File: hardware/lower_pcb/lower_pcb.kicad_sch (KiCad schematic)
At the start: 0 parts

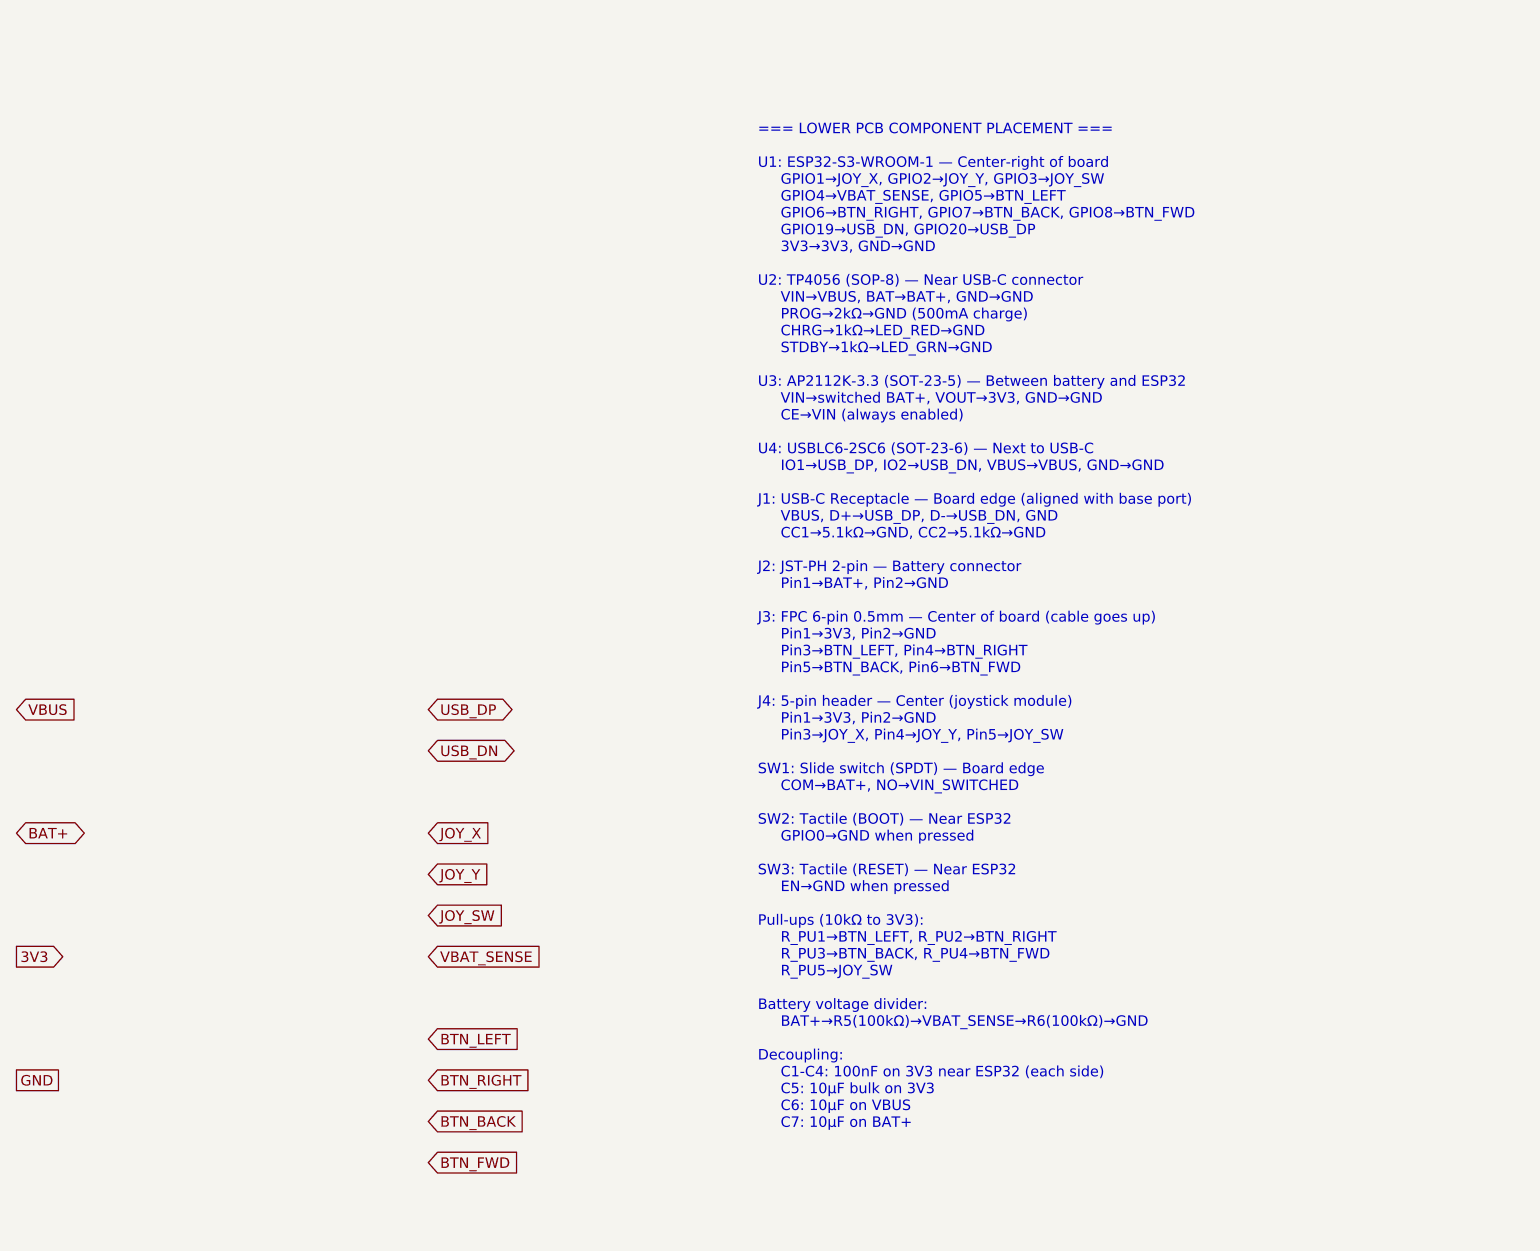
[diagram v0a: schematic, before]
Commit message: fix: move BTN pull-ups (R1-R4) to upper PCB; update schematics + BOM
- upper_pcb.kicad_sch rev 1.2: add R1-R4 (10k pull-ups) + C1 (100nF)
- lower_pcb.kicad_sch rev 1.1: remove R_PU1-R_PU4, keep R_PU5 for JOY_SW
- docs/BOM.md: updated refs to match new placement
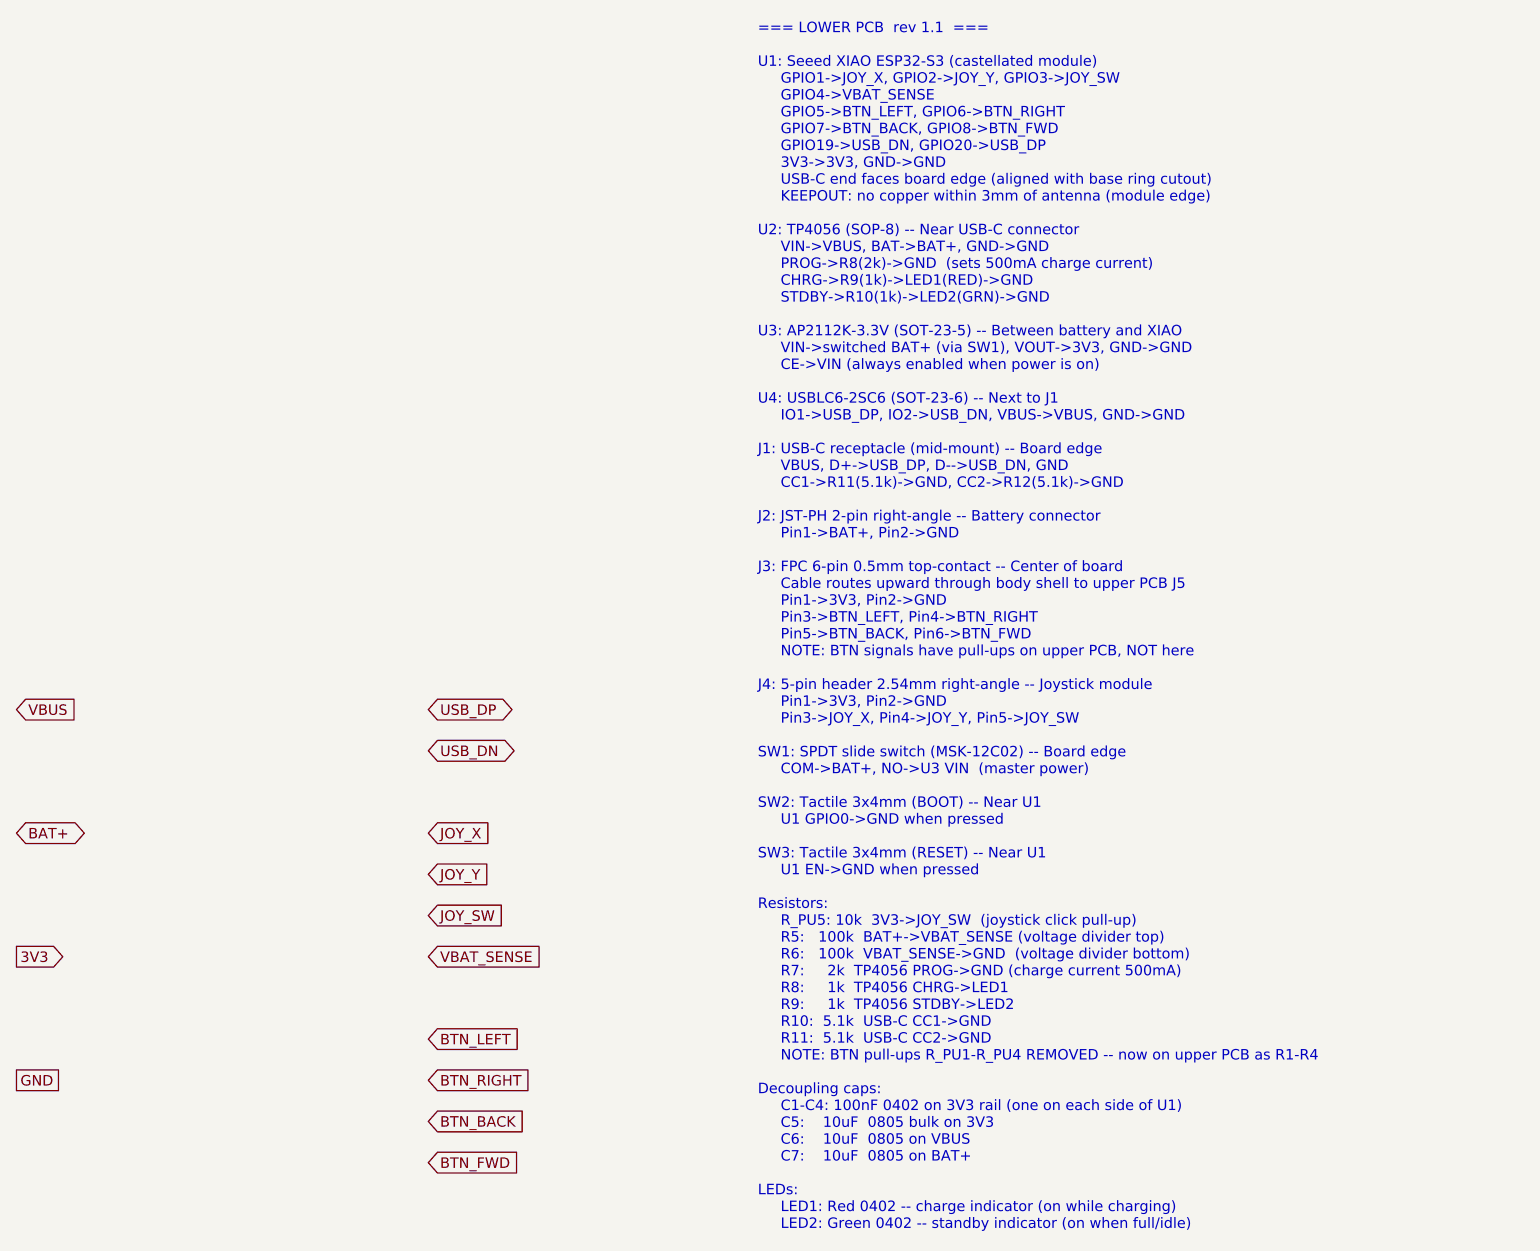
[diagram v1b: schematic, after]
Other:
- note added: "=== LOWER PCB rev 1.1 === U1: Seeed XIAO ESP32-S3 (castellated module) GPIO1->JOY_X, GPIO2->JOY_Y, GPIO3->JOY_SW GPIO4->VBAT_SENSE GPIO5->BTN_LEFT, GPIO6->BTN_RIGHT GPIO7->BTN_BACK, GPIO8->BTN_FWD GPIO19->USB_DN, GPIO20->USB_DP 3V3->3V3, GND->GND USB-C end faces board edge (aligned with base ring cutout) KEEPOUT: no copper within 3mm of antenna (module edge) U2: TP4056 (SOP-8) -- Near USB-C conne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"
- note removed: "=== LOWER PCB COMPONENT PLACEMENT === U1: ESP32-S3-WROOM-1 — Center-right of board GPIO1→JOY_X, GPIO2→JOY_Y, GPIO3→JOY_SW GPIO4→VBAT_SENSE, GPIO5→BTN_LEFT GPIO6→BTN_RIGHT, GPIO7→BTN_BACK, GPIO8→BTN_FWD GPIO19→USB_DN, GPIO20→USB_DP 3V3→3V3, GND→GND U2: TP4056 (SOP-8) — Near USB-C connector VIN→VBUS, BAT→BAT+, GND→GND PROG→2kΩ→GND (500mA charge) CHRG→1kΩ→LED_RED→GND STDBY→1kΩ→LED_GRN→GND U3: AP2112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"
- title: DaPao Space Mouse — Lower PCB -> DaPao Space Mouse - Lower PCB
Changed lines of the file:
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@@
   (paper "A3")
   (title_block
-    (title "DaPao Space Mouse — Lower PCB")
-    (date "2026-03-11")
-    (rev "1.0")
-    (comment 1 "Base board: ESP32-S3 + Power + Joystick + FPC")
-    (comment 2 "Circular PCB ∅88mm, 2-layer")
+    (title "DaPao Space Mouse - Lower PCB")
+    (date "2026-03-20")
+    (rev "1.1")
+    (comment 1 "Base board: XIAO ESP32-S3 + Power + Joystick + FPC")
+    (comment 2 "Circular PCB dia88mm, 2-layer, 1.6mm thick")
+    (comment 3 "Rev 1.1: BTN pull-ups moved to upper PCB (R1-R4). R_PU5 (JOY_SW) stays here.")
   )
-  ;; ============================================================
-  ;; This schematic defines the netlist and component references
-  ;; for the lower (base) PCB. Open in KiCad 7+ schematic editor,
-  ;; then assign footprints and place symbols interactively.
-  ;;
-  ;; Components are placed as text annotations for reference.
-  ;; Use "Place Symbol" in KiCad to add each from the library.
-  ;; ============================================================
   ;; --- POWER NETS ---
   (global_label "VBUS" (shape input) (at 30 40 0)
@@
   )
   ;; --- SIGNAL NETS ---
-  (global_label "USB_DP" (shape bidirectional) (at 80 40 0)
-    (effects (font (size 1.27 1.27)))
-  )
-  (global_label "USB_DN" (shape bidirectional) (at 80 45 0)
-    (effects (font (size 1.27 1.27)))
-  )
-  (global_label "JOY_X" (shape input) (at 80 55 0)
-    (effects (font (size 1.27 1.27)))
-  )
-  (global_label "JOY_Y" (shape input) (at 80 60 0)
-    (effects (font (size 1.27 1.27)))
-  )
-  (global_label "JOY_SW" (shape input) (at 80 65 0)
-    (effects (font (size 1.27 1.27)))
-  )
-  (global_label "VBAT_SENSE" (shape input) (at 80 70 0)
-    (effects (font (size 1.27 1.27)))
-  )
-  (global_label "BTN_LEFT" (shape input) (at 80 80 0)
-    (effects (font (size 1.27 1.27)))
-  )
-  (global_label "BTN_RIGHT" (shape input) (at 80 85 0)
-    (effects (font (size 1.27 1.27)))
-  )
-  (global_label "BTN_BACK" (shape input) (at 80 90 0)
-    (effects (font (size 1.27 1.27)))
-  )
-  (global_label "BTN_FWD" (shape input) (at 80 95 0)
-    (effects (font (size 1.27 1.27)))
-  )
-  ;; --- TEXT ANNOTATIONS (component placement guide) ---
-  (text "=== LOWER PCB COMPONENT PLACEMENT ===\n\nU1: ESP32-S3-WROOM-1 — Center-right of board\n     GPIO1→JOY_X, GPIO2→JOY_Y, GPIO3→JOY_SW\n     GPIO4→VBAT_SENSE, GPIO5→BTN_LEFT\n     GPIO6→BTN_RIGHT, GPIO7→BTN_BACK, GPIO8→BTN_FWD\n     GPIO19→USB_DN, GPIO20→USB_DP\n     3V3→3V3, GND→GND\n\nU2: TP4056 (SOP-8) — Near USB-C connector\n     VIN→VBUS, BAT→BAT+, GND→GND\n     PROG→2kΩ→GND (500mA charge)\n     CHRG→1kΩ→LED_RED→GND\n     STDBY→1kΩ→LED_GRN→GND\n\nU3: AP2112K-3.3 (SOT-23-5) — Between battery and ESP32\n     VIN→switched BAT+, VOUT→3V3, GND→GND\n     CE→VIN (always enabled)\n\nU4: USBLC6-2SC6 (SOT-23-6) — Next to USB-C\n     IO1→USB_DP, IO2→USB_DN, VBUS→VBUS, GND→GND\n\nJ1: USB-C Receptacle — Board edge (aligned with base port)\n     VBUS, D+→USB_DP, D-→USB_DN, GND\n     CC1→5.1kΩ→GND, CC2→5.1kΩ→GND\n\nJ2: JST-PH 2-pin — Battery connector\n     Pin1→BAT+, Pin2→GND\n\nJ3: FPC 6-pin 0.5mm — Center of board (cable goes up)\n     Pin1→3V3, Pin2→GND\n     Pin3→BTN_LEFT, Pin4→BTN_RIGHT\n     Pin5→BTN_BACK, Pin6→BTN_FWD\n\nJ4: 5-pin header — Center (joystick module)\n     Pin1→3V3, Pin2→GND\n     Pin3→JOY_X, Pin4→JOY_Y, Pin5→JOY_SW\n\nSW1: Slide switch (SPDT) — Board edge\n     COM→BAT+, NO→VIN_SWITCHED\n\nSW2: Tactile (BOOT) — Near ESP32\n     GPIO0→GND when pressed\n\nSW3: Tactile (RESET) — Near ESP32\n     EN→GND when pressed\n\nPull-ups (10kΩ to 3V3):\n     R_PU1→BTN_LEFT, R_PU2→BTN_RIGHT\n     R_PU3→BTN_BACK, R_PU4→BTN_FWD\n     R_PU5→JOY_SW\n\nBattery voltage divider:\n     BAT+→R5(100kΩ)→VBAT_SENSE→R6(100kΩ)→GND\n\nDecoupling:\n     C1-C4: 100nF on 3V3 near ESP32 (each side)\n     C5: 10µF bulk on 3V3\n     C6: 10µF on VBUS\n     C7: 10µF on BAT+"
+  (global_label "USB_DP"     (shape bidirectional) (at 80 40 0) (effects (font (size 1.27 1.27))))
+  (global_label "USB_DN"     (shape bidirectional) (at 80 45 0) (effects (font (size 1.27 1.27))))
+  (global_label "JOY_X"      (shape input) (at 80 55 0) (effects (font (size 1.27 1.27))))
+  (global_label "JOY_Y"      (shape input) (at 80 60 0) (effects (font (size 1.27 1.27))))
+  (global_label "JOY_SW"     (shape input) (at 80 65 0) (effects (font (size 1.27 1.27))))
+  (global_label "VBAT_SENSE" (shape input) (at 80 70 0) (effects (font (size 1.27 1.27))))
+  (global_label "BTN_LEFT"   (shape input) (at 80 80 0) (effects (font (size 1.27 1.27))))
+  (global_label "BTN_RIGHT"  (shape input) (at 80 85 0) (effects (font (size 1.27 1.27))))
+  (global_label "BTN_BACK"   (shape input) (at 80 90 0) (effects (font (size 1.27 1.27))))
+  (global_label "BTN_FWD"    (shape input) (at 80 95 0) (effects (font (size 1.27 1.27))))
+  ;; --- COMPONENT PLACEMENT & WIRING NOTES ---
+  (text "=== LOWER PCB  rev 1.1  ===\n\nU1: Seeed XIAO ESP32-S3 (castellated module)\n     GPIO1->JOY_X, GPIO2->JOY_Y, GPIO3->JOY_SW\n     GPIO4->VBAT_SENSE\n     GPIO5->BTN_LEFT, GPIO6->BTN_RIGHT\n     GPIO7->BTN_BACK, GPIO8->BTN_FWD\n     GPIO19->USB_DN, GPIO20->USB_DP\n     3V3->3V3, GND->GND\n     USB-C end faces board edge (aligned with base ring cutout)\n     KEEPOUT: no copper within 3mm of antenna (module edge)\n\nU2: TP4056 (SOP-8) -- Near USB-C connector\n     VIN->VBUS, BAT->BAT+, GND->GND\n     PROG->R8(2k)->GND  (sets 500mA charge current)\n     CHRG->R9(1k)->LED1(RED)->GND\n     STDBY->R10(1k)->LED2(GRN)->GND\n\nU3: AP2112K-3.3V (SOT-23-5) -- Between battery and XIAO\n     VIN->switched BAT+ (via SW1), VOUT->3V3, GND->GND\n     CE->VIN (always enabled when power is on)\n\nU4: USBLC6-2SC6 (SOT-23-6) -- Next to J1\n     IO1->USB_DP, IO2->USB_DN, VBUS->VBUS, GND->GND\n\nJ1: USB-C receptacle (mid-mount) -- Board edge\n     VBUS, D+->USB_DP, D-->USB_DN, GND\n     CC1->R11(5.1k)->GND, CC2->R12(5.1k)->GND\n\nJ2: JST-PH 2-pin right-angle -- Battery connector\n     Pin1->BAT+, Pin2->GND\n\nJ3: FPC 6-pin 0.5mm top-contact -- Center of board\n     Cable routes upward through body shell to upper PCB J5\n     Pin1->3V3, Pin2->GND\n     Pin3->BTN_LEFT, Pin4->BTN_RIGHT\n     Pin5->BTN_BACK, Pin6->BTN_FWD\n     NOTE: BTN signals have pull-ups on upper PCB, NOT here\n\nJ4: 5-pin header 2.54mm right-angle -- Joystick module\n     Pin1->3V3, Pin2->GND\n     Pin3->JOY_X, Pin4->JOY_Y, Pin5->JOY_SW\n\nSW1: SPDT slide switch (MSK-12C02) -- Board edge\n     COM->BAT+, NO->U3 VIN  (master power)\n\nSW2: Tactile 3x4mm (BOOT) -- Near U1\n     U1 GPIO0->GND when pressed\n\nSW3: Tactile 3x4mm (RESET) -- Near U1\n     U1 EN->GND when pressed\n\nResistors:\n     R_PU5: 10k  3V3->JOY_SW  (joystick click pull-up)\n     R5:   100k  BAT+->VBAT_SENSE (voltage divider top)\n     R6:   100k  VBAT_SENSE->GND  (voltage divider bottom)\n     R7:     2k  TP4056 PROG->GND (charge current 500mA)\n     R8:     1k  TP4056 CHRG->LED1\n     R9:     1k  TP4056 STDBY->LED2\n     R10:  5.1k  USB-C CC1->GND\n     R11:  5.1k  USB-C CC2->GND\n     NOTE: BTN pull-ups R_PU1-R_PU4 REMOVED -- now on upper PCB as R1-R4\n\nDecoupling caps:\n     C1-C4: 100nF 0402 on 3V3 rail (one on each side of U1)\n     C5:    10uF  0805 bulk on 3V3\n     C6:    10uF  0805 on VBUS\n     C7:    10uF  0805 on BAT+\n\nLEDs:\n     LED1: Red 0402 -- charge indicator (on while charging)\n     LED2: Green 0402 -- standby indicator (on when full/idle)"
     (at 120 30 0)
     (effects (font (size 1.27 1.27)) (justify left))
